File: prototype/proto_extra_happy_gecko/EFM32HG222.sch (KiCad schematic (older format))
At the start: 1 part

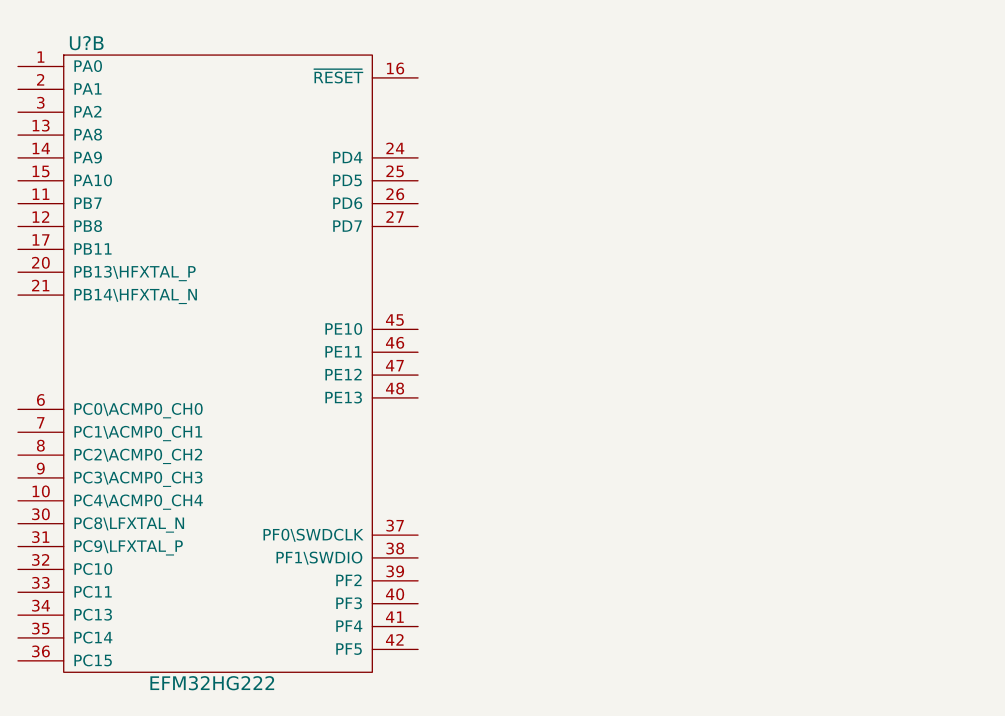
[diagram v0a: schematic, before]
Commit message: Added all leds, 3.3Vreg, and routed busses
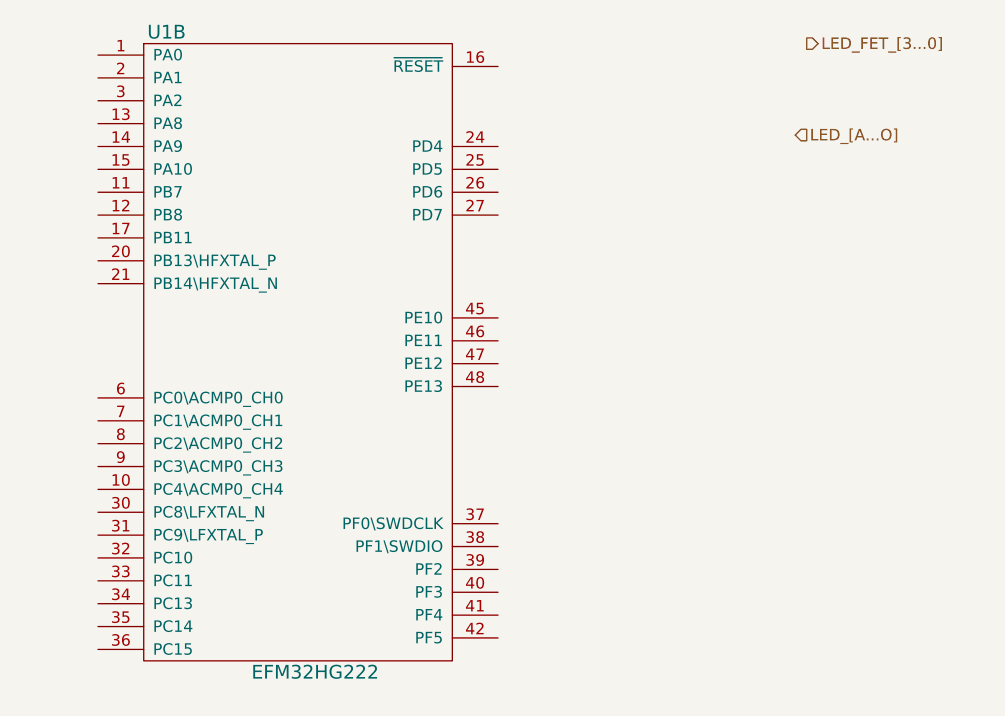
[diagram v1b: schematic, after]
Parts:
- removed U?: EFM32HG222, symbol EFM32HG222
- added U1: EFM32HG222, symbol EFM32HG222
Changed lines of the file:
@@
 LIBS:xtal
 LIBS:capacitors
-LIBS:inductor
 LIBS:mosfet
 LIBS:led
 LIBS:resistor
+LIBS:TLC5954
+LIBS:watch_led
+LIBS:watch_pmos
+LIBS:inductor
+LIBS:regulators
 LIBS:proto_extra_happy_gecko-cache
 EELAYER 25 0
@@
 $EndDescr
 $Comp
-L EFM32HG222 U?
-U 2 1 58E1275E
-P 5200 2850
-F 0 "U?" H 4650 4050 60  0000 C CNN
-F 1 "EFM32HG222" H 5200 1250 60  0000 C CNN
-F 2 "" H 4450 3500 60  0000 C CNN
-F 3 "" H 4550 3600 60  0000 C CNN
-F 4 "EFM32HG222F64G-B-QFP48" H 5000 2900 60  0001 C CNN "PART #"
-F 5 "SILICON LABS" H 5000 3000 60  0001 C CNN "MANUFACTURER"
-	2    5200 2850
+L EFM32HG222 U1
+U 2 1 590A172E
+P 5550 2800
+F 0 "U1" H 5000 4000 60  0000 C CNN
+F 1 "EFM32HG222" H 5575 1450 60  0001 C CNN
+F 2 "" H 4900 3900 60  0000 C CNN
+F 3 "" H 5000 4000 60  0000 C CNN
+F 4 "EFM32HG222F64G-B-QFP48" H 5450 3300 60  0001 C CNN "PART #"
+F 5 "SILICON LABS" H 5450 3400 60  0001 C CNN "MANUFACTURER"
+F 6 "EFM32HG222" H 5650 1200 60  0000 C CNN "PART_SHORT"
+	2    5550 2800
 	1    0    0    -1
 $EndComp
+Text HLabel 7800 1650 2    50   Output ~ 0
+LED_FET_[3...0]
+Text HLabel 7750 2050 2    50   Input ~ 0
+LED_[A...O]
 $EndSCHEMATC
